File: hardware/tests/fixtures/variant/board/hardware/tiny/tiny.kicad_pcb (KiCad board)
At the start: 2 copper layers, 40 x 10 mm, 7 parts

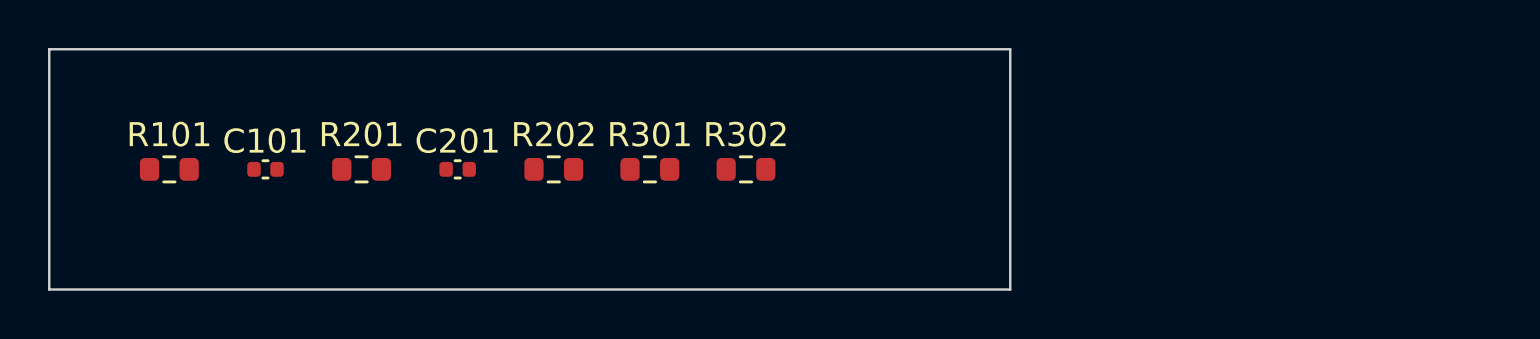
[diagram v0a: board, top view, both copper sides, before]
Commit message: odapkit variant: absent-state check and software outputs per variant (RFC 0011 rules 2, 7, 8)
The absent-state check reads the XML netlist with the variant's resolution: every
net a dnp block touches is classified with the fitted parts only (single-pin,
floating, rail without source, defined) and matched to a declared absent state
from the block sheets' interface tables or the record's absent_state list; nets
touched only by other unfitted parts are reported when they become single-pin.
Findings absent.floating, absent.single-pin, absent.rail-unsourced,
absent.undeclared, absent.declared-mismatch and absent.not-applicable.

apply writes absent-state.json (opendap.variant-absent-state/v1),
software/capabilities.json (opendap.variant-capabilities/v1, a fragment for the
device description; consumer side open) and software/devicetree.json
(opendap.variant-devicetree/v1) with variant.dtso, status okay or disabled per
block node, blocks with no node listed as skipped. check runs the absent-state
check per variant. Block records gain structured absent_state and software;
the Markdown catalog reads its Absent state and Software rows. The fixture's
sensor sheet carries an interface table.

Co-Authored-By: Claude Opus 5.5 <noreply@anthropic.com>
Claude-Session: https://claude.ai/code/session_01Ei262h3TpgY9vyfNLMi5Mn
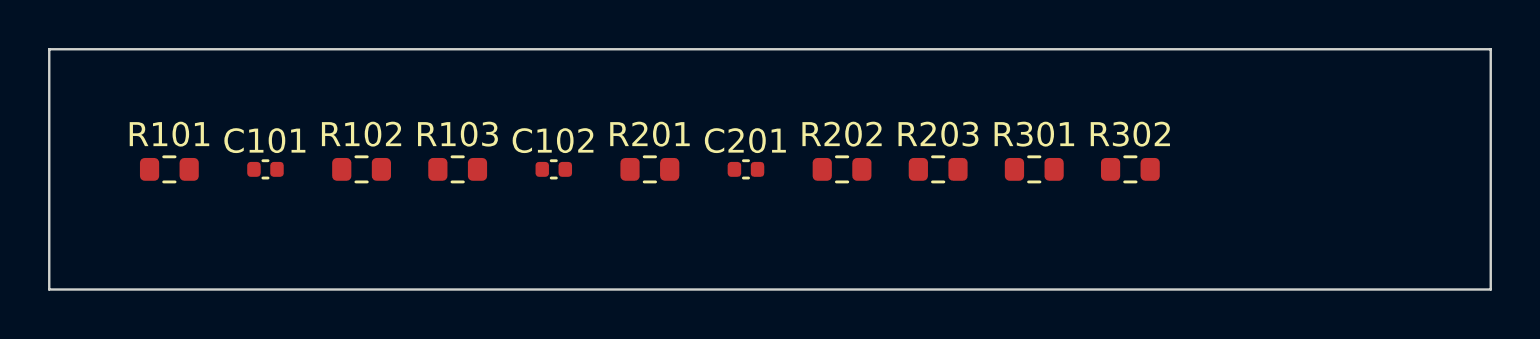
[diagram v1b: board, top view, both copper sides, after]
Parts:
- removed the R201 at (18.0, 10.0)
- added C102: 100 nF, Capacitor_SMD:C_0402_1005Metric, F.Cu at (26.0, 10.0)
- added R102: 100 kΩ, Resistor_SMD:R_0603_1608Metric, F.Cu at (18.0, 10.0)
- added R103: 4.7 kΩ, Resistor_SMD:R_0603_1608Metric, F.Cu at (22.0, 10.0)
- added R203: 1 kΩ, Resistor_SMD:R_0603_1608Metric, F.Cu at (42.0, 10.0)
- added R301: MEM-32, Resistor_SMD:R_0603_1608Metric, F.Cu at (46.0, 10.0)
- R201: renamed from R301; value MEM-32 -> 4.7 kΩ
- moved R302 16.0 mm to (50.0, 10.0)
- moved C201 12.0 mm to (34.0, 10.0)
- moved R202 12.0 mm to (38.0, 10.0)
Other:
- board size 40 x 10 mm -> 60 x 10 mm
